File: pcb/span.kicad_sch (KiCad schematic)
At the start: 80 parts, among them J1 MJ-4PP-9, J2 MJ-4PP-9, J3 OLED, J4 OLED, SW1 SW_PUSH, SW10 SW_PUSH, SW11 SW_PUSH, SW12 SW_PUSH, SW13 SW_PUSH, SW14 SW_PUSH, SW15 SW_PUSH, SW16 SW_PUSH, SW17 SW_PUSH, SW18 SW_PUSH, SW19 SW_PUSH, SW2 SW_PUSH, SW20 SW_PUSH, SW21 SW_PUSH, SW22 SW_PUSH, SW23 SW_PUSH, SW24 SW_PUSH, SW25 SW_PUSH, SW26 SW_PUSH, SW27 SW_PUSH, SW28 SW_PUSH, SW29 SW_PUSH, SW3 SW_PUSH, SW30 SW_PUSH, SW31 SW_PUSH, SW32 SW_PUSH, SW33 SW_PUSH, SW34 SW_PUSH, SW35 SW_PUSH, SW36 SW_PUSH, SW4 SW_PUSH, SW5 SW_PUSH, SW6 SW_PUSH, SW7 SW_PUSH, SW8 SW_PUSH, SW9 SW_PUSH, U1 ProMicro, U2 ProMicro

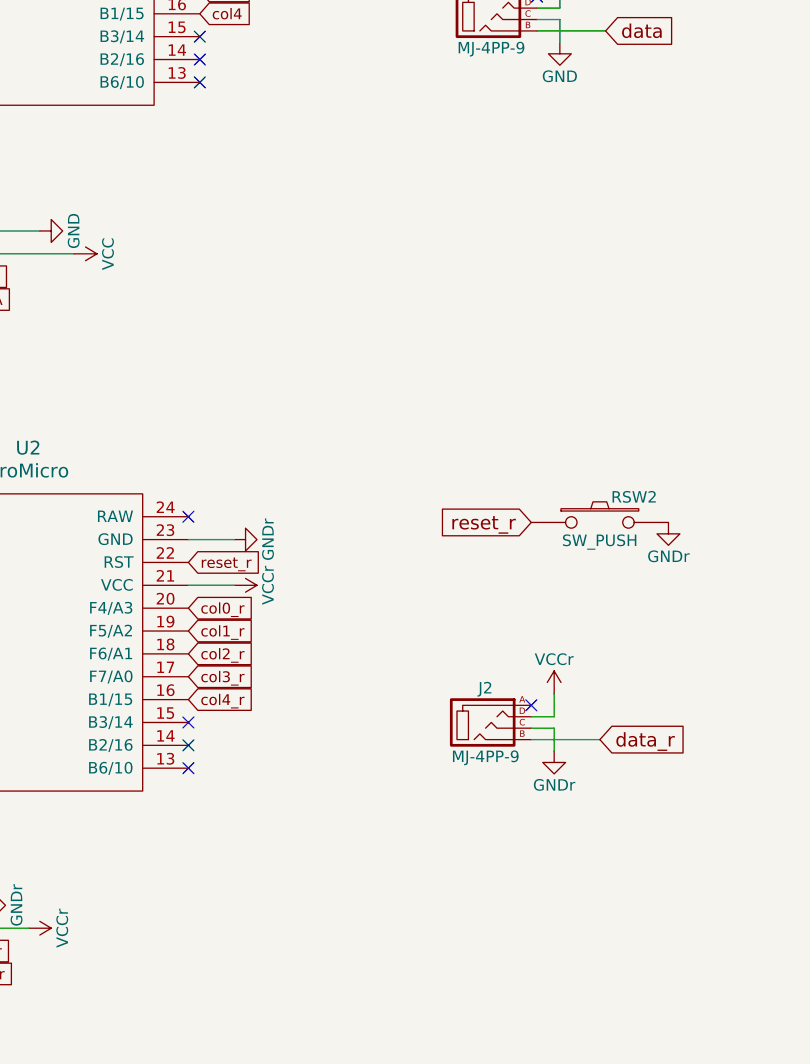
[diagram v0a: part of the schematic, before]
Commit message: pcb: use slightly bigger holes for the controller pins and  mounting holes
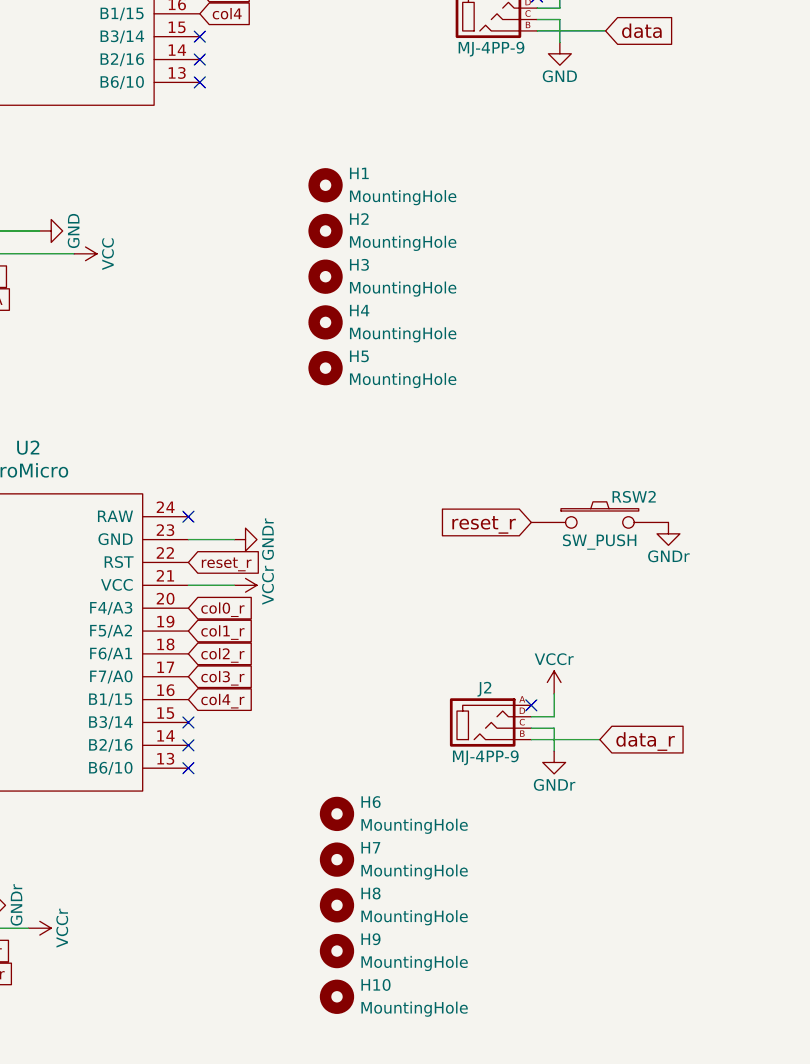
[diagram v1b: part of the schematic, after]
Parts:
- added H1, H10, H2, H3, H4, H5, H6, H7, H8, H9: MountingHole, holykeebs:M2_SPACER, symbol Mechanical:MountingHole
- U1, U2: footprint kbd:ProMicro_v3 -> holykeebs:ProMicro_1mm_holes
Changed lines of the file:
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@@
+    )
+  )
+  (symbol (lib_id "Mechanical:MountingHole") (at 187.96 67.31 0) (unit 1)
+    (in_bom yes) (on_board yes) (dnp no) (fields_autoplaced)
+    (property "Reference" "H2" (at 190.5 66.04 0)
+      (effects (font (size 1.27 1.27)) (justify left))
+    )
+    (property "Value" "MountingHole" (at 190.5 68.58 0)
+      (effects (font (size 1.27 1.27)) (justify left))
+    )
+    (property "Footprint" "holykeebs:M2_SPACER" (at 187.96 67.31 0)
+      (effects (font (size 1.27 1.27)) hide)
+    )
+    (property "Datasheet" "~" (at 187.96 67.31 0)
+      (effects (font (size 1.27 1.27)) hide)
+    )
+    (instances
+      (project "span"
+        (path "/e1bb6603-5312-4208-8a34-43c6ce03c5a1"
+          (reference "H2") (unit 1)
+        )
+      )
     )
   )
@@
         (path "/e1bb6603-5312-4208-8a34-43c6ce03c5a1"
           (reference "SW35") (unit 1)
+        )
+      )
+    )
+  )
+  (symbol (lib_id "Mechanical:MountingHole") (at 189.23 132.08 0) (unit 1)
+    (in_bom yes) (on_board yes) (dnp no) (fields_autoplaced)
+    (property "Reference" "H6" (at 191.77 130.81 0)
+      (effects (font (size 1.27 1.27)) (justify left))
+    )
+    (property "Value" "MountingHole" (at 191.77 133.35 0)
+      (effects (font (size 1.27 1.27)) (justify left))
+    )
+    (property "Footprint" "holykeebs:M2_SPACER" (at 189.23 132.08 0)
+      (effects (font (size 1.27 1.27)) hide)
+    )
+    (property "Datasheet" "~" (at 189.23 132.08 0)
+      (effects (font (size 1.27 1.27)) hide)
+    )
+    (instances
+      (project "span"
+        (path "/e1bb6603-5312-4208-8a34-43c6ce03c5a1"
+          (reference "H6") (unit 1)
         )
       )
@@
     )
   )
+  (symbol (lib_id "Mechanical:MountingHole") (at 187.96 72.39 0) (unit 1)
+    (in_bom yes) (on_board yes) (dnp no) (fields_autoplaced)
+    (property "Reference" "H3" (at 190.5 71.12 0)
+      (effects (font (size 1.27 1.27)) (justify left))
+    )
+    (property "Value" "MountingHole" (at 190.5 73.66 0)
+      (effects (font (size 1.27 1.27)) (justify left))
+    )
+    (property "Footprint" "holykeebs:M2_SPACER" (at 187.96 72.39 0)
+      (effects (font (size 1.27 1.27)) hide)
+    )
+    (property "Datasheet" "~" (at 187.96 72.39 0)
+      (effects (font (size 1.27 1.27)) hide)
+    )
+    (instances
+      (project "span"
+        (path "/e1bb6603-5312-4208-8a34-43c6ce03c5a1"
+          (reference "H3") (unit 1)
+        )
+      )
+    )
+  )
   (symbol (lib_id "power:GND") (at 132.08 106.68 270) (unit 1)
     (in_bom yes) (on_board yes) (dnp no)
@@
         (path "/e1bb6603-5312-4208-8a34-43c6ce03c5a1"
           (reference "#PWR014") (unit 1)
+        )
+      )
+    )
+  )
+  (symbol (lib_id "Mechanical:MountingHole") (at 187.96 77.47 0) (unit 1)
+    (in_bom yes) (on_board yes) (dnp no) (fields_autoplaced)
+    (property "Reference" "H4" (at 190.5 76.2 0)
+      (effects (font (size 1.27 1.27)) (justify left))
+    )
+    (property "Value" "MountingHole" (at 190.5 78.74 0)
+      (effects (font (size 1.27 1.27)) (justify left))
+    )
+    (property "Footprint" "holykeebs:M2_SPACER" (at 187.96 77.47 0)
+      (effects (font (size 1.27 1.27)) hide)
+    )
+    (property "Datasheet" "~" (at 187.96 77.47 0)
+      (effects (font (size 1.27 1.27)) hide)
+    )
+    (instances
+      (project "span"
+        (path "/e1bb6603-5312-4208-8a34-43c6ce03c5a1"
+          (reference "H4") (unit 1)
         )
       )
@@
     )
   )
+  (symbol (lib_id "Mechanical:MountingHole") (at 189.23 147.32 0) (unit 1)
+    (in_bom yes) (on_board yes) (dnp no) (fields_autoplaced)
+    (property "Reference" "H9" (at 191.77 146.05 0)
+      (effects (font (size 1.27 1.27)) (justify left))
+    )
+    (property "Value" "MountingHole" (at 191.77 148.59 0)
+      (effects (font (size 1.27 1.27)) (justify left))
+    )
+    (property "Footprint" "holykeebs:M2_SPACER" (at 189.23 147.32 0)
+      (effects (font (size 1.27 1.27)) hide)
+    )
+    (property "Datasheet" "~" (at 189.23 147.32 0)
+      (effects (font (size 1.27 1.27)) hide)
+    )
+    (instances
+      (project "span"
+        (path "/e1bb6603-5312-4208-8a34-43c6ce03c5a1"
+          (reference "H9") (unit 1)
+        )
+      )
+    )
+  )
   (symbol (lib_id "Device:D") (at 30.48 137.16 90) (unit 1)
     (in_bom yes) (on_board yes) (dnp no)
@@
       (effects (font (size 1.524 1.524)))
     )
-    (property "Footprint" "kbd:ProMicro_v3" (at 157.48 139.7 0)
+    (property "Footprint" "holykeebs:ProMicro_1mm_holes" (at 157.48 139.7 0)
       (effects (font (size 1.524 1.524)) hide)
     )
@@
     )
   )
+  (symbol (lib_id "Mechanical:MountingHole") (at 189.23 152.4 0) (unit 1)
+    (in_bom yes) (on_board yes) (dnp no) (fields_autoplaced)
+    (property "Reference" "H10" (at 191.77 151.13 0)
+      (effects (font (size 1.27 1.27)) (justify left))
+    )
+    (property "Value" "MountingHole" (at 191.77 153.67 0)
+      (effects (font (size 1.27 1.27)) (justify left))
+    )
+    (property "Footprint" "holykeebs:M2_SPACER" (at 189.23 152.4 0)
+      (effects (font (size 1.27 1.27)) hide)
+    )
+    (property "Datasheet" "~" (at 189.23 152.4 0)
+      (effects (font (size 1.27 1.27)) hide)
+    )
+    (instances
+      (project "span"
+        (path "/e1bb6603-5312-4208-8a34-43c6ce03c5a1"
+          (reference "H10") (unit 1)
+        )
+      )
+    )
+  )
+  (symbol (lib_id "Mechanical:MountingHole") (at 187.96 82.55 0) (unit 1)
+    (in_bom yes) (on_board yes) (dnp no) (fields_autoplaced)
+    (property "Reference" "H5" (at 190.5 81.28 0)
+      (effects (font (size 1.27 1.27)) (justify left))
+    )
+    (property "Value" "MountingHole" (at 190.5 83.82 0)
+      (effects (font (size 1.27 1.27)) (justify left))
+    )
+    (property "Footprint" "holykeebs:M2_SPACER" (at 187.96 82.55 0)
+      (effects (font (size 1.27 1.27)) hide)
+    )
+    (property "Datasheet" "~" (at 187.96 82.55 0)
+      (effects (font (size 1.27 1.27)) hide)
+    )
+    (instances
+      (project "span"
+        (path "/e1bb6603-5312-4208-8a34-43c6ce03c5a1"
+          (reference "H5") (unit 1)
+        )
+      )
+    )
+  )
   (symbol (lib_id "power:VCC") (at 177.8 106.68 270) (unit 1)
     (in_bom yes) (on_board yes) (dnp no)
@@
         (path "/e1bb6603-5312-4208-8a34-43c6ce03c5a1"
           (reference "SW25") (unit 1)
+        )
+      )
+    )
+  )
+  (symbol (lib_id "Mechanical:MountingHole") (at 189.23 142.24 0) (unit 1)
+    (in_bom yes) (on_board yes) (dnp no) (fields_autoplaced)
+    (property "Reference" "H8" (at 191.77 140.97 0)
+      (effects (font (size 1.27 1.27)) (justify left))
+    )
+    (property "Value" "MountingHole" (at 191.77 143.51 0)
+      (effects (font (size 1.27 1.27)) (justify left))
+    )
+    (property "Footprint" "holykeebs:M2_SPACER" (at 189.23 142.24 0)
+      (effects (font (size 1.27 1.27)) hide)
+    )
+    (property "Datasheet" "~" (at 189.23 142.24 0)
+      (effects (font (size 1.27 1.27)) hide)
+    )
+    (instances
+      (project "span"
+        (path "/e1bb6603-5312-4208-8a34-43c6ce03c5a1"
+          (reference "H8") (unit 1)
         )
       )
@@
         (path "/e1bb6603-5312-4208-8a34-43c6ce03c5a1"
           (reference "D24") (unit 1)
+        )
+      )
+    )
+  )
+  (symbol (lib_id "Mechanical:MountingHole") (at 189.23 137.16 0) (unit 1)
+    (in_bom yes) (on_board yes) (dnp no) (fields_autoplaced)
+    (property "Reference" "H7" (at 191.77 135.89 0)
+      (effects (font (size 1.27 1.27)) (justify left))
+    )
+    (property "Value" "MountingHole" (at 191.77 138.43 0)
+      (effects (font (size 1.27 1.27)) (justify left))
+    )
+    (property "Footprint" "holykeebs:M2_SPACER" (at 189.23 137.16 0)
+      (effects (font (size 1.27 1.27)) hide)
+    )
+    (property "Datasheet" "~" (at 189.23 137.16 0)
+      (effects (font (size 1.27 1.27)) hide)
+    )
+    (instances
+      (project "span"
+        (path "/e1bb6603-5312-4208-8a34-43c6ce03c5a1"
+          (reference "H7") (unit 1)
         )
       )
@@
       (effects (font (size 1.524 1.524)))
     )
-    (property "Footprint" "kbd:ProMicro_v3" (at 158.75 63.5 0)
+    (property "Footprint" "holykeebs:ProMicro_1mm_holes" (at 158.75 63.5 0)
       (effects (font (size 1.524 1.524)) hide)
     )
@@
         )
       )
+    )
+  )
+  (symbol (lib_id "Mechanical:MountingHole") (at 187.96 62.23 0) (unit 1)
+    (in_bom yes) (on_board yes) (dnp no) (fields_autoplaced)
+    (property "Reference" "H1" (at 190.5 60.96 0)
+      (effects (font (size 1.27 1.27)) (justify left))
+    )
+    (property "Value" "MountingHole" (at 190.5 63.5 0)
+      (effects (font (size 1.27 1.27)) (justify left))
+    )
+    (property "Footprint" "holykeebs:M2_SPACER" (at 187.96 62.23 0)
+      (effects (font (size 1.27 1.27)) hide)
+    )
+    (property "Datasheet" "~" (at 187.96 62.23 0)
+      (effects (font (size 1.27 1.27)) hide)
+    )
+    (instances
+      (project "span"
+        (path "/e1bb6603-5312-4208-8a34-43c6ce03c5a1"
+          (reference "H1") (unit 1)
+        )
+      )

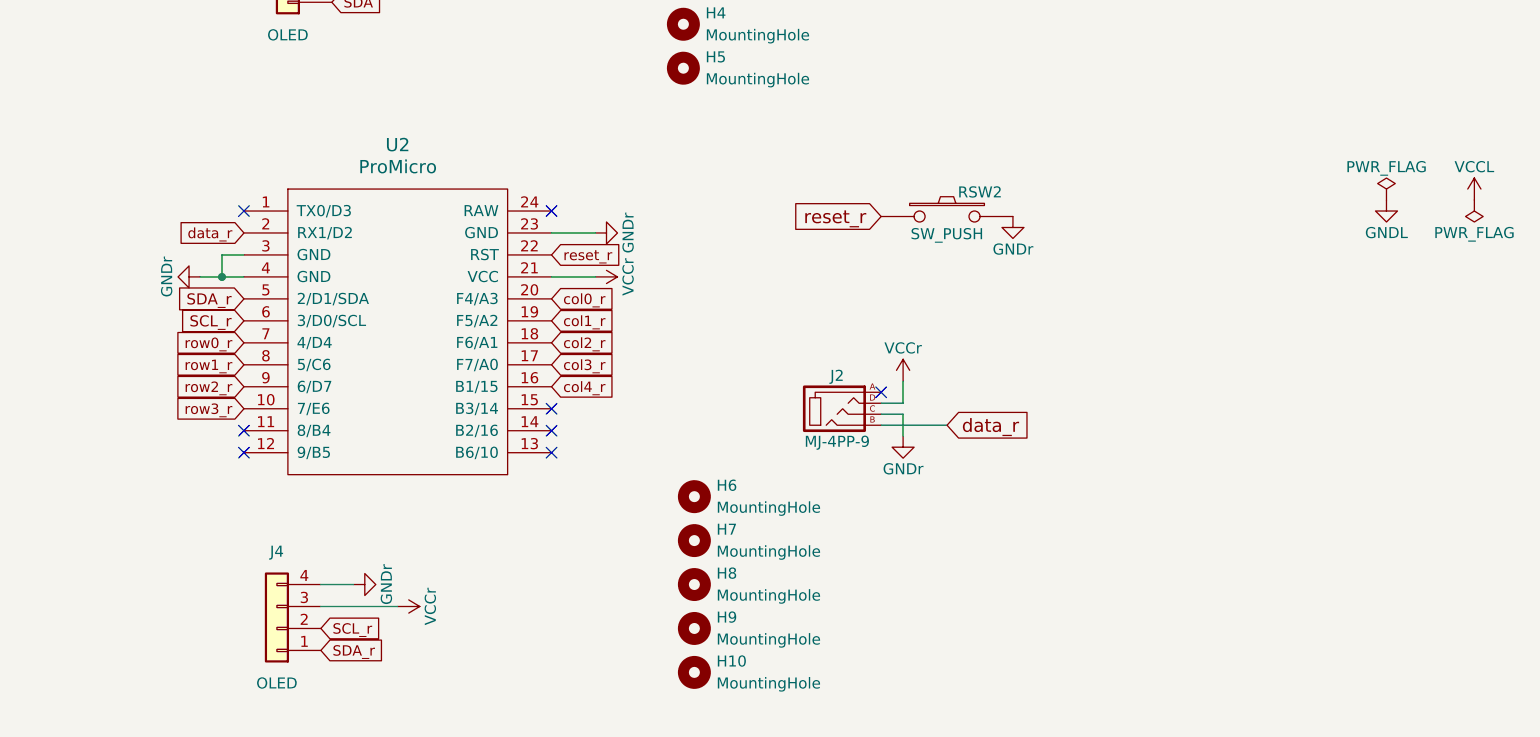
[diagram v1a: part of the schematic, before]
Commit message: pcb: add filled zones
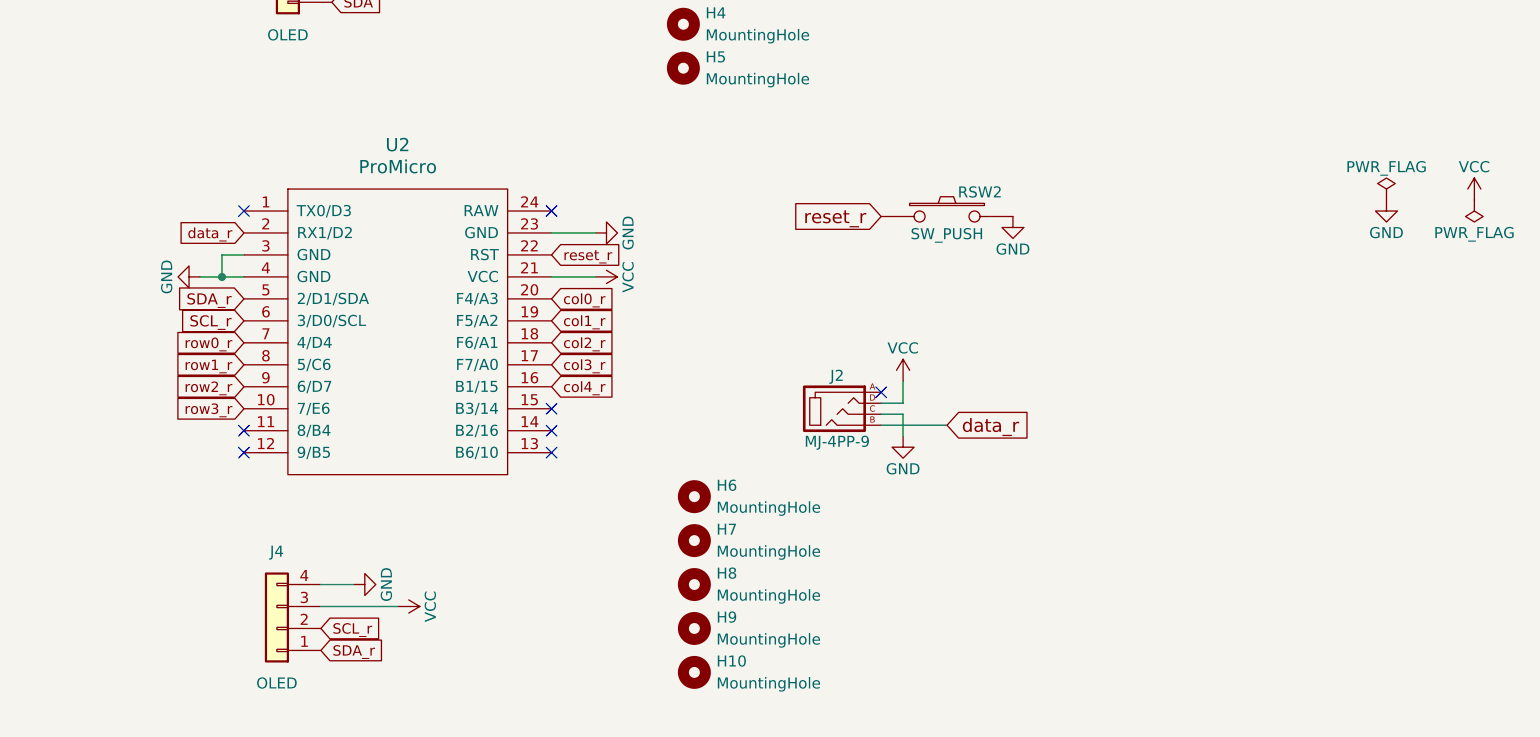
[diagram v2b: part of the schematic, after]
